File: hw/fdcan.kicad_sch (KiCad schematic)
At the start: 1 part, among them U5 TCAN334G

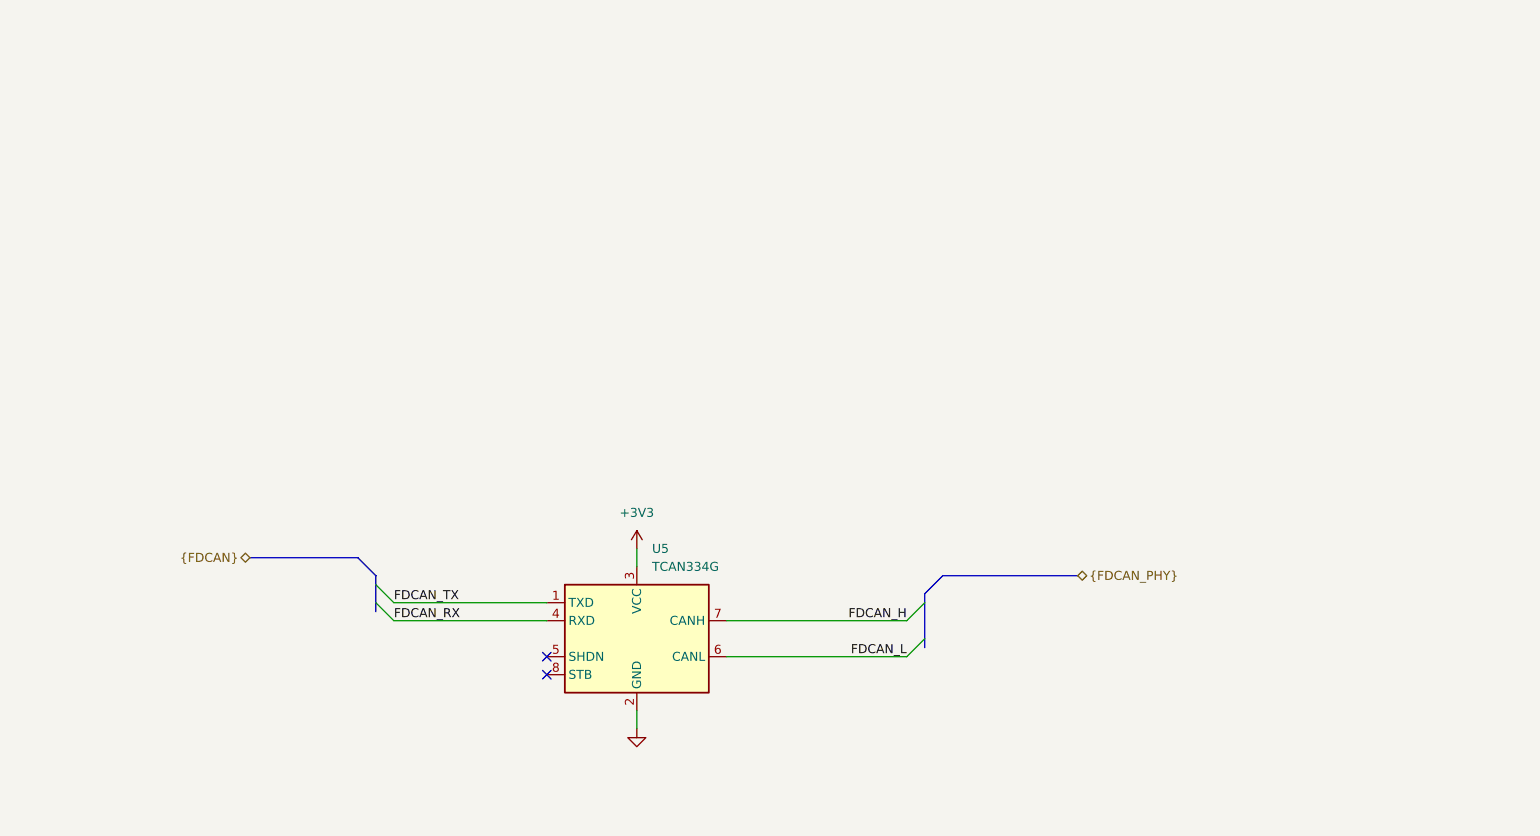
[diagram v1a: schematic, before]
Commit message: cleaned up *.kicad_sch
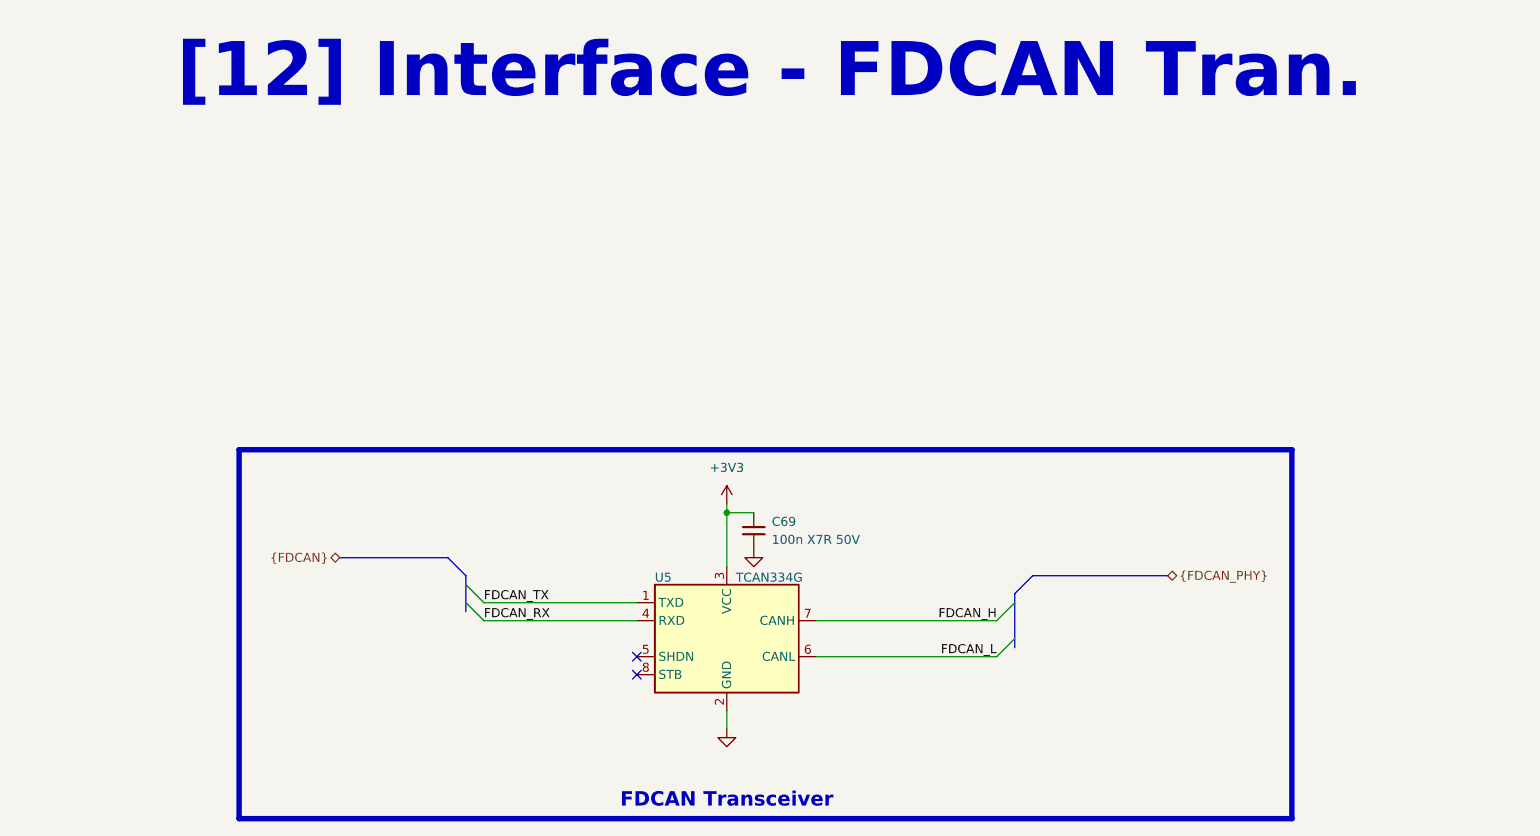
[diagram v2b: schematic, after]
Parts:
- added C69: 100n X7R 50V, Capacitor_SMD:C_0603_1608Metric, symbol Device:C_Small
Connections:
- net +3V3: now also C69.1
- net GND: now also C69.2
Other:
- note added: "FDCAN Transceiver"
- note added: "[12] Interface - FDCAN Tran."
- moved on the sheet: U5
